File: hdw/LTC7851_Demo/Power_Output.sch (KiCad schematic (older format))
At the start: 0 parts

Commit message: Assigned some custom footprints
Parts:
- added J? (x2): +5V OUT, Custom Footprints Library:Wuerth_7461096_M4_Shank_9pos, symbol Connector:Screw_Terminal_01x01
- added J? (x2): GND OUT, Custom Footprints Library:Wuerth_7461096_M4_Shank_9pos, symbol Connector:Screw_Terminal_01x01
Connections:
- net labels added: +5V, GND
- wire segments 0 -> 8
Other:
- note added: "Place bulk output caps close to terminals"
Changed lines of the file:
@@
 Comment4 ""
 $EndDescr
+$Comp
+L Connector:Screw_Terminal_01x01 J?
+U 1 1 5BC3341B
+P 5520 2650
+F 0 "J?" H 5520 2750 50  0000 C CNN
+F 1 "+5V OUT" H 5520 2550 50  0000 C CNN
+F 2 "Custom Footprints Library:Wuerth_7461096_M4_Shank_9pos" H 5520 2650 50  0001 C CNN
+F 3 "~" H 5520 2650 50  0001 C CNN
+	1    5520 2650
+	1    0    0    -1
+$EndComp
+$Comp
+L Connector:Screw_Terminal_01x01 J?
+U 1 1 5BC33AA7
+P 5520 2950
+F 0 "J?" H 5520 3050 50  0000 C CNN
+F 1 "+5V OUT" H 5520 2850 50  0000 C CNN
+F 2 "Custom Footprints Library:Wuerth_7461096_M4_Shank_9pos" H 5520 2950 50  0001 C CNN
+F 3 "~" H 5520 2950 50  0001 C CNN
+	1    5520 2950
+	1    0    0    -1
+$EndComp
+$Comp
+L power:+5V #PWR?
+U 1 1 5BC33B1C
+P 5240 2570
+F 0 "#PWR?" H 5240 2420 50  0001 C CNN
+F 1 "+5V" H 5240 2710 50  0000 C CNN
+F 2 "" H 5240 2570 50  0001 C CNN
+F 3 "" H 5240 2570 50  0001 C CNN
+	1    5240 2570
+	1    0    0    -1
+$EndComp
+Wire Wire Line
+	5240 2570 5240 2650
+Wire Wire Line
+	5240 2650 5320 2650
+Wire Wire Line
+	5240 2650 5240 2950
+Wire Wire Line
+	5240 2950 5320 2950
+Connection ~ 5240 2650
+$Comp
+L Connector:Screw_Terminal_01x01 J?
+U 1 1 5BC33E64
+P 5520 3280
+F 0 "J?" H 5520 3380 50  0000 C CNN
+F 1 "GND OUT" H 5520 3180 50  0000 C CNN
+F 2 "Custom Footprints Library:Wuerth_7461096_M4_Shank_9pos" H 5520 3280 50  0001 C CNN
+F 3 "~" H 5520 3280 50  0001 C CNN
+	1    5520 3280
+	1    0    0    -1
+$EndComp
+$Comp
+L Connector:Screw_Terminal_01x01 J?
+U 1 1 5BC341B2
+P 5520 3570
+F 0 "J?" H 5520 3670 50  0000 C CNN
+F 1 "GND OUT" H 5520 3470 50  0000 C CNN
+F 2 "Custom Footprints Library:Wuerth_7461096_M4_Shank_9pos" H 5520 3570 50  0001 C CNN
+F 3 "~" H 5520 3570 50  0001 C CNN
+	1    5520 3570
+	1    0    0    -1
+$EndComp
+$Comp
+L power:GND #PWR?
+U 1 1 5BC34225
+P 5240 3650
+F 0 "#PWR?" H 5240 3400 50  0001 C CNN
+F 1 "GND" H 5240 3500 50  0000 C CNN
+F 2 "" H 5240 3650 50  0001 C CNN
+F 3 "" H 5240 3650 50  0001 C CNN
+	1    5240 3650
+	1    0    0    -1
+$EndComp
+Wire Wire Line
+	5240 3650 5240 3570
+Wire Wire Line
+	5240 3570 5320 3570
+Wire Wire Line
+	5240 3570 5240 3280
+Wire Wire Line
+	5240 3280 5320 3280
+Connection ~ 5240 3570
+Text Notes 3340 3220 0    50   ~ 0
+Place bulk output caps close to terminals
 $EndSCHEMATC

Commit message: Annotated schematic
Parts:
- gave numbers to parts that had none: 4
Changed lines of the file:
@@
 $EndDescr
 $Comp
-L Connector:Screw_Terminal_01x01 J?
+L Connector:Screw_Terminal_01x01 J901
 U 1 1 5BC3341B
 P 5520 2650
-F 0 "J?" H 5520 2750 50  0000 C CNN
+F 0 "J901" H 5520 2750 50  0000 C CNN
 F 1 "+5V OUT" H 5520 2550 50  0000 C CNN
 F 2 "Custom Footprints Library:Wuerth_7461096_M4_Shank_9pos" H 5520 2650 50  0001 C CNN
@@
 $EndComp
 $Comp
-L Connector:Screw_Terminal_01x01 J?
+L Connector:Screw_Terminal_01x01 J902
 U 1 1 5BC33AA7
 P 5520 2950
-F 0 "J?" H 5520 3050 50  0000 C CNN
+F 0 "J902" H 5520 3050 50  0000 C CNN
 F 1 "+5V OUT" H 5520 2850 50  0000 C CNN
 F 2 "Custom Footprints Library:Wuerth_7461096_M4_Shank_9pos" H 5520 2950 50  0001 C CNN
@@
 $EndComp
 $Comp
-L power:+5V #PWR?
+L power:+5V #PWR0901
 U 1 1 5BC33B1C
 P 5240 2570
-F 0 "#PWR?" H 5240 2420 50  0001 C CNN
+F 0 "#PWR0901" H 5240 2420 50  0001 C CNN
 F 1 "+5V" H 5240 2710 50  0000 C CNN
 F 2 "" H 5240 2570 50  0001 C CNN
@@
 Connection ~ 5240 2650
 $Comp
-L Connector:Screw_Terminal_01x01 J?
+L Connector:Screw_Terminal_01x01 J903
 U 1 1 5BC33E64
 P 5520 3280
-F 0 "J?" H 5520 3380 50  0000 C CNN
+F 0 "J903" H 5520 3380 50  0000 C CNN
 F 1 "GND OUT" H 5520 3180 50  0000 C CNN
 F 2 "Custom Footprints Library:Wuerth_7461096_M4_Shank_9pos" H 5520 3280 50  0001 C CNN
@@
 $EndComp
 $Comp
-L Connector:Screw_Terminal_01x01 J?
+L Connector:Screw_Terminal_01x01 J904
 U 1 1 5BC341B2
 P 5520 3570
-F 0 "J?" H 5520 3670 50  0000 C CNN
+F 0 "J904" H 5520 3670 50  0000 C CNN
 F 1 "GND OUT" H 5520 3470 50  0000 C CNN
 F 2 "Custom Footprints Library:Wuerth_7461096_M4_Shank_9pos" H 5520 3570 50  0001 C CNN
@@
 $EndComp
 $Comp
-L power:GND #PWR?
+L power:GND #PWR0902
 U 1 1 5BC34225
 P 5240 3650
-F 0 "#PWR?" H 5240 3400 50  0001 C CNN
+F 0 "#PWR0902" H 5240 3400 50  0001 C CNN
 F 1 "GND" H 5240 3500 50  0000 C CNN
 F 2 "" H 5240 3650 50  0001 C CNN

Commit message: Added Digi-Key part numbers for all parts
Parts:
- J901, J902, J903, J904: Digi-Key PN (none) -> 732-3214-ND
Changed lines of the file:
@@
 F 2 "Custom Footprints Library:Wuerth_7461096_M4_Shank_9pos" H 5520 2650 50  0001 C CNN
 F 3 "~" H 5520 2650 50  0001 C CNN
+F 4 "732-3214-ND" H 0   0   50  0001 C CNN "Digi-Key PN"
 	1    5520 2650
 	1    0    0    -1
@@
 F 2 "Custom Footprints Library:Wuerth_7461096_M4_Shank_9pos" H 5520 2950 50  0001 C CNN
 F 3 "~" H 5520 2950 50  0001 C CNN
+F 4 "732-3214-ND" H 0   0   50  0001 C CNN "Digi-Key PN"
 	1    5520 2950
 	1    0    0    -1
@@
 F 2 "Custom Footprints Library:Wuerth_7461096_M4_Shank_9pos" H 5520 3280 50  0001 C CNN
 F 3 "~" H 5520 3280 50  0001 C CNN
+F 4 "732-3214-ND" H 0   0   50  0001 C CNN "Digi-Key PN"
 	1    5520 3280
 	1    0    0    -1
@@
 F 2 "Custom Footprints Library:Wuerth_7461096_M4_Shank_9pos" H 5520 3570 50  0001 C CNN
 F 3 "~" H 5520 3570 50  0001 C CNN
+F 4 "732-3214-ND" H 0   0   50  0001 C CNN "Digi-Key PN"
 	1    5520 3570
 	1    0    0    -1

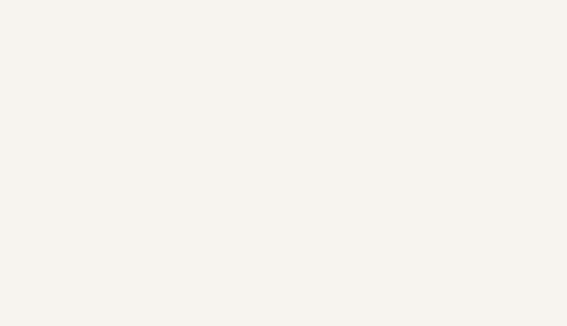
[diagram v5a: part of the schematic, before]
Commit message: Added page titles
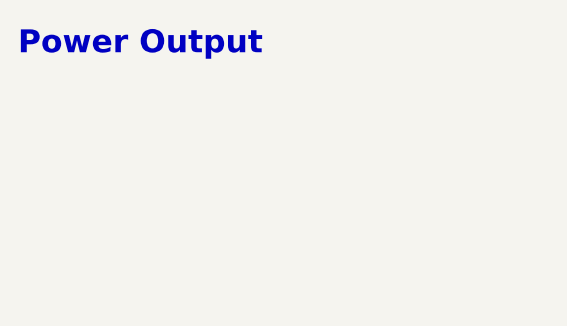
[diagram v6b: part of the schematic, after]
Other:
- note added: "Power Output"
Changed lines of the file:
@@
 Text Notes 3340 3220 0    50   ~ 0
 Place bulk output caps close to terminals
+Text Notes 540  690  0    100  ~ 20
+Power Output
 $EndSCHEMATC
